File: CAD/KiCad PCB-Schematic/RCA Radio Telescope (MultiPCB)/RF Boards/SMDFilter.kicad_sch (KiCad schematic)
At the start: 3 parts, among them J16 ANT, J17 ANT, U16 BPF-A1340+

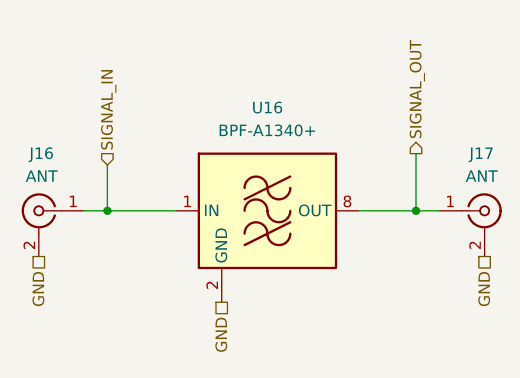
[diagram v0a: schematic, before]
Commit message: RF Boards Redo (WIP)
- Overhauling current RF boards to keep 4 RF boards in total
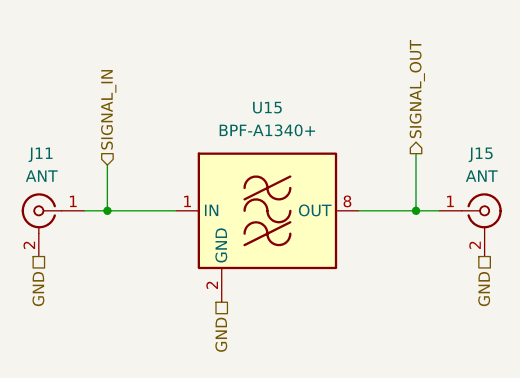
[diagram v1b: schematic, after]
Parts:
- removed J16, J17: ANT, Library:CONN_142-0711-821_CIN, symbol Connector:Conn_Coaxial
- removed U16: BPF-A1340+, RF_Mini-Circuits:Mini-Circuits_HQ1157, symbol RF_Filter:BPF-A355
- added J11, J15: ANT, Library:CONN_142-0711-821_CIN, symbol Connector:Conn_Coaxial
- added U15: BPF-A1340+, RF_Mini-Circuits:Mini-Circuits_HQ1157, symbol RF_Filter:BPF-A355
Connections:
- net GND: now also J11.2 (Ext), J15.2 (Ext), U15.10 (GND), U15.11 (GND), U15.12 (GND), U15.13 (GND), U15.14 (GND), U15.2 (GND), U15.3 (GND), U15.4 (GND), U15.5 (GND), U15.6 (GND), U15.7 (GND), U15.9 (GND)
- net SIGNAL_IN: now also J11.1 (In), U15.1 (IN)
- net SIGNAL_OUT: now also J15.1 (In), U15.8 (OUT)
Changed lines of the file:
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@@
+		)
+	)
+	(hierarchical_label "SIGNAL_OUT"
+		(shape output)
+		(at 77.47 49.53 90)
+		(effects
+			(font
+				(size 1.27 1.27)
+			)
+			(justify left)
+		)
+	)
+	(hierarchical_label "GND"
+		(shape passive)
+		(at 35.56 60.96 270)
+		(effects
+			(font
+				(size 1.27 1.27)
+			)
+			(justify right)
+		)
+	)
+	(hierarchical_label "SIGNAL_IN"
+		(shape input)
+		(at 43.18 50.8 90)
+		(effects
+			(font
+				(size 1.27 1.27)
+			)
+			(justify left)
+		)
+	)
+	(hierarchical_label "GND"
+		(shape passive)
+		(at 55.88 66.04 270)
+		(effects
+			(font
+				(size 1.27 1.27)
+			)
+			(justify right)
 		)
 	)
@@
 			)
 			(justify right)
-		)
-	)
-	(hierarchical_label "GND"
-		(shape passive)
-		(at 55.88 66.04 270)
-		(effects
-			(font
-				(size 1.27 1.27)
-			)
-			(justify right)
-		)
-	)
-	(hierarchical_label "GND"
-		(shape passive)
-		(at 35.56 60.96 270)
-		(effects
-			(font
-				(size 1.27 1.27)
-			)
-			(justify right)
-		)
-	)
-	(hierarchical_label "SIGNAL_IN"
-		(shape input)
-		(at 43.18 50.8 90)
-		(effects
-			(font
-				(size 1.27 1.27)
-			)
-			(justify left)
-		)
-	)
-	(hierarchical_label "SIGNAL_OUT"
-		(shape output)
-		(at 77.47 49.53 90)
-		(effects
-			(font
-				(size 1.27 1.27)
-			)
-			(justify left)
 		)
 	)
@@
 		(on_board yes)
 		(dnp no)
-		(property "Reference" "J17"
+		(property "Reference" "J15"
 			(at 84.7726 49.53 0)
 			(effects
@@
 		(instances
 			(project "RCA Radio Telescope"
-				(path "/1630c5ee-b70a-455e-85ba-86a73955b8fd/ed1ef573-f899-48e8-bb37-c5537adb3c53"
-					(reference "J17")
-					(unit 1)
-				)
-			)
-		)
-	)
-	(symbol
-		(lib_id "RF_Filter:BPF-A355")
-		(at 60.96 55.88 0)
-		(unit 1)
-		(exclude_from_sim no)
-		(in_bom yes)
-		(on_board yes)
-		(dnp no)
-		(fields_autoplaced yes)
-		(property "Reference" "U16"
-			(at 60.96 44.45 0)
-			(effects
-				(font
-					(size 1.27 1.27)
-				)
-			)
-		)
-		(property "Value" "BPF-A1340+"
-			(at 60.96 46.99 0)
-			(effects
-				(font
-					(size 1.27 1.27)
-				)
-			)
-		)
-		(property "Footprint" "RF_Mini-Circuits:Mini-Circuits_HQ1157"
-			(at 60.96 68.58 0)
-			(effects
-				(font
-					(size 1.27 1.27)
-				)
-				(hide yes)
-			)
-		)
-		(property "Datasheet" "https://www.minicircuits.com/pdfs/BPF-A355+.pdf"
-			(at 60.96 53.34 0)
-			(effects
-				(font
-					(size 1.27 1.27)
-				)
-				(hide yes)
-			)
-		)
-		(property "Description" "Bandpass Filter, 310 to 400 MHz, 50 Ohm, Mini-Circuits HQ1157"
-			(at 60.96 55.88 0)
-			(effects
-				(font
-					(size 1.27 1.27)
-				)
-				(hide yes)
-			)
-		)
-		(pin "3"
-		)
-		(pin "9"
-		)
-		(pin "12"
-		)
-		(pin "13"
-		)
-		(pin "6"
-		)
-		(pin "4"
-		)
-		(pin "10"
-		)
-		(pin "7"
-		)
-		(pin "11"
-		)
-		(pin "14"
-		)
-		(pin "1"
-		)
-		(pin "5"
-		)
-		(pin "8"
-		)
-		(pin "2"
-		)
-		(instances
-			(project "RCA Radio Telescope"
-				(path "/1630c5ee-b70a-455e-85ba-86a73955b8fd/ed1ef573-f899-48e8-bb37-c5537adb3c53"
-					(reference "U16")
+				(path "/1630c5ee-b70a-455e-85ba-86a73955b8fd/b1bd03bb-513c-4075-8ea8-0ed535b26dec"
+					(reference "J15")
 					(unit 1)
 				)
@@
 		(dnp no)
 		(fields_autoplaced yes)
-		(property "Reference" "J16"
+		(property "Reference" "J11"
 			(at 35.8774 49.53 0)
 			(effects
@@
 		(instances
 			(project "RCA Radio Telescope"
-				(path "/1630c5ee-b70a-455e-85ba-86a73955b8fd/ed1ef573-f899-48e8-bb37-c5537adb3c53"
-					(reference "J16")
+				(path "/1630c5ee-b70a-455e-85ba-86a73955b8fd/b1bd03bb-513c-4075-8ea8-0ed535b26dec"
+					(reference "J11")
 					(unit 1)
 				)
+			)
+		)
+	)
+	(symbol
+		(lib_id "RF_Filter:BPF-A355")
+		(at 60.96 55.88 0)
+		(unit 1)
+		(exclude_from_sim no)
+		(in_bom yes)
+		(on_board yes)
+		(dnp no)
+		(fields_autoplaced yes)
+		(property "Reference" "U15"
+			(at 60.96 44.45 0)
+			(effects
+				(font
+					(size 1.27 1.27)
+				)
+			)
+		)
+		(property "Value" "BPF-A1340+"
+			(at 60.96 46.99 0)
+			(effects
+				(font
+					(size 1.27 1.27)
+				)
+			)
+		)
+		(property "Footprint" "RF_Mini-Circuits:Mini-Circuits_HQ1157"
+			(at 60.96 68.58 0)
+			(effects
+				(font
+					(size 1.27 1.27)
+				)
+				(hide yes)
+			)
+		)
+		(property "Datasheet" "https://www.minicircuits.com/pdfs/BPF-A355+.pdf"
+			(at 60.96 53.34 0)
+			(effects
+				(font
+					(size 1.27 1.27)
+				)
+				(hide yes)
+			)
+		)
+		(property "Description" "Bandpass Filter, 310 to 400 MHz, 50 Ohm, Mini-Circuits HQ1157"
+			(at 60.96 55.88 0)
+			(effects
+				(font
+					(size 1.27 1.27)
+				)
+				(hide yes)
+			)
+		)
+		(pin "3"
+		)
+		(pin "9"
+		)
+		(pin "12"
+		)
+		(pin "13"
+		)
+		(pin "6"
+		)
+		(pin "4"
+		)
+		(pin "10"
+		)
+		(pin "7"
+		)
+		(pin "11"
+		)
+		(pin "14"
+		)
+		(pin "1"
+		)
+		(pin "5"
+		)
+		(pin "8"
+		)
+		(pin "2"
+		)
+		(instances
+			(project "RCA Radio Telescope"
+				(path "/1630c5ee-b70a-455e-85ba-86a73955b8fd/b1bd03bb-513c-4075-8ea8-0ed535b26dec"
+					(reference "U15")
+					(unit 1)
+				)
